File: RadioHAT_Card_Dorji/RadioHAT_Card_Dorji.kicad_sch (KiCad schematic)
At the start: 10 parts, among them J2 Conn_Coaxial, J3 Conn_Coaxial, J4 Conn_Coaxial, J5 Conn_Coaxial, J6 Conn_Coaxial

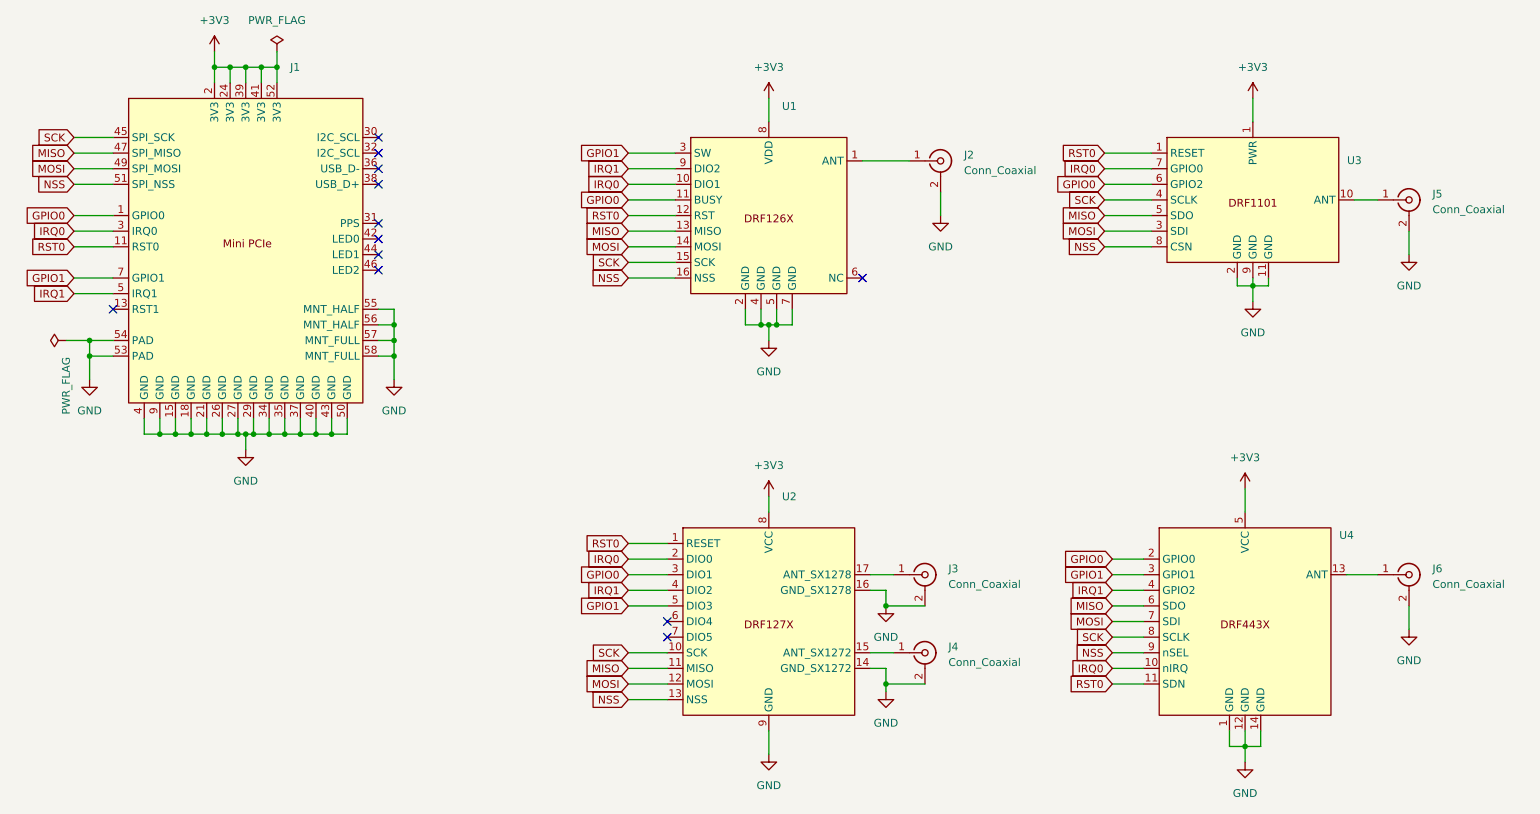
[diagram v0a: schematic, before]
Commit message: [PCB] Minor Dorji card fixes from rev0
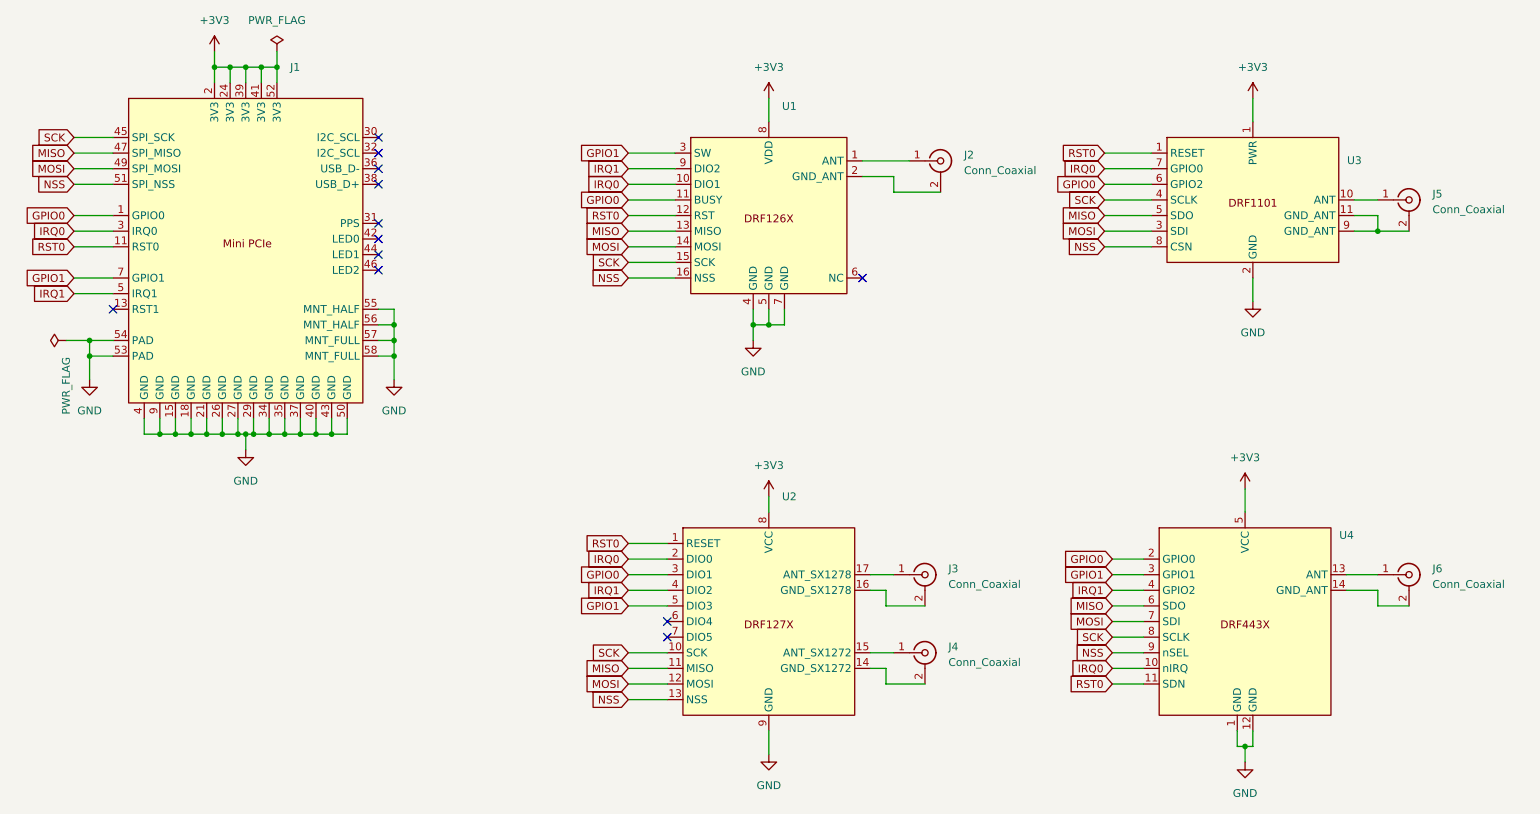
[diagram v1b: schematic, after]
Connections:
- net GND: no longer J2.2 (Ext), J3.2 (Ext), J4.2 (Ext), J5.2 (Ext), J6.2 (Ext), U1.2 (GND), U2.14 (GND_SX1272), U2.16 (GND_SX1278), U3.11 (GND), U3.9 (GND), U4.14 (GND)
- new net: J4.2 (Ext), U2.14 (GND_SX1272)
- new net: J3.2 (Ext), U2.16 (GND_SX1278)
- new net: J2.2 (Ext), U1.2 (GND_ANT)
- new net: J6.2 (Ext), U4.14 (GND_ANT)
- new net: J5.2 (Ext), U3.11 (GND_ANT), U3.9 (GND_ANT)

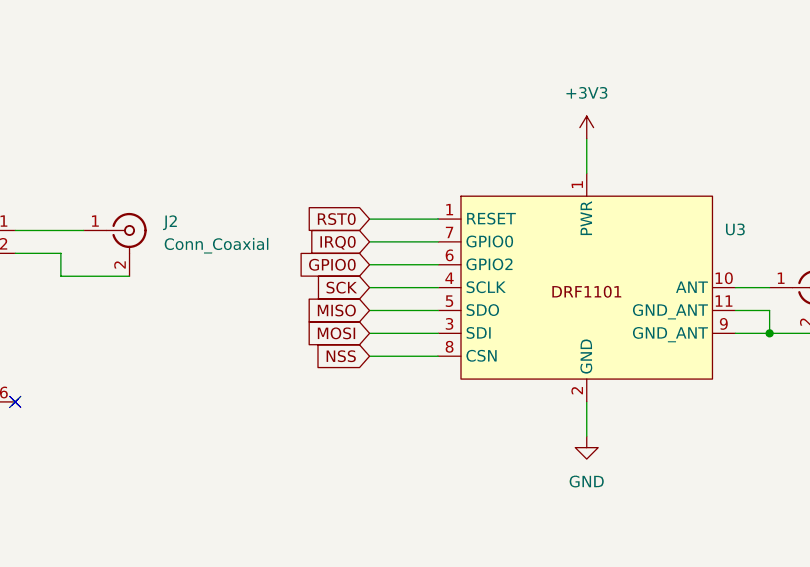
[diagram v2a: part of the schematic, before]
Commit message: Fix ERC issues
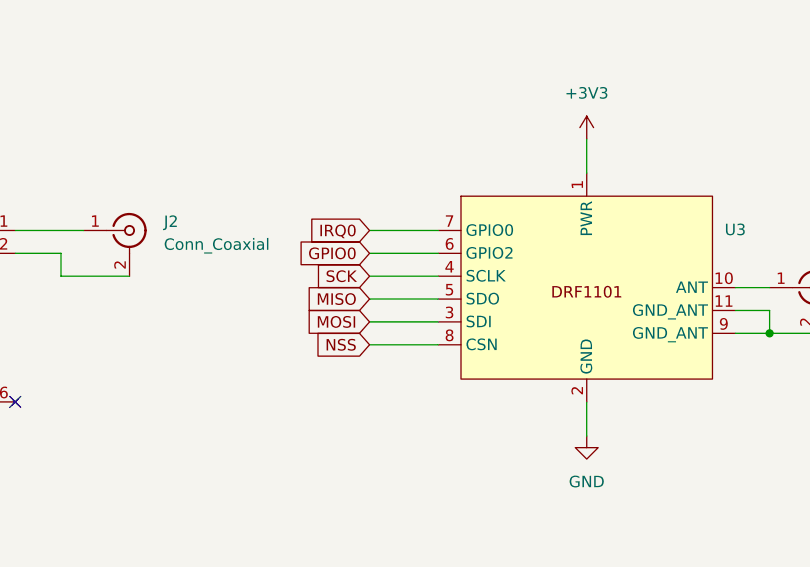
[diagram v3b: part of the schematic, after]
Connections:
- net RST0: no longer U3.1 (PWR)

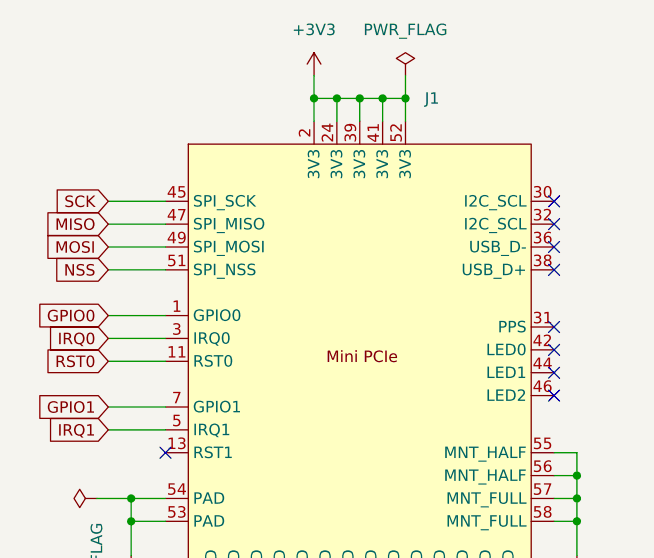
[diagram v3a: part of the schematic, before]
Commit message: Update symbols to align with library
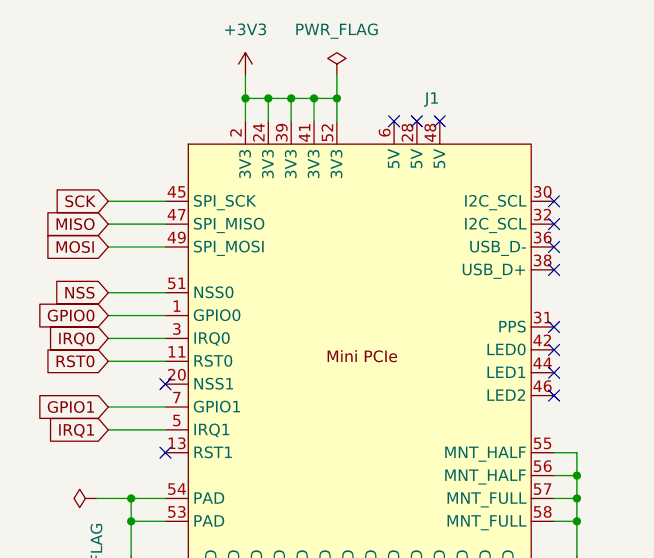
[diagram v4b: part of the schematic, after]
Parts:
- J1: Mouser (none) -> 571-1775838-2
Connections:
- no-connect marks 12 -> 16
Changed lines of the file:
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@@
 	(paper "A4")
 	(junction
-		(at 54.61 29.21)
-		(diameter 0)
-		(color 0 0 0 0)
-	)
-	(junction
 		(at 142.24 71.12)
 		(diameter 0)
@@
 	)
 	(junction
-		(at 62.23 29.21)
+		(at 52.07 29.21)
 		(diameter 0)
 		(color 0 0 0 0)
@@
 	)
 	(junction
-		(at 52.07 29.21)
-		(diameter 0)
-		(color 0 0 0 0)
-	)
-	(junction
-		(at 59.69 29.21)
+		(at 58.42 88.9)
 		(diameter 0)
 		(color 0 0 0 0)
 	)
 	(junction
-		(at 58.42 88.9)
+		(at 48.26 88.9)
 		(diameter 0)
 		(color 0 0 0 0)
 	)
 	(junction
-		(at 48.26 88.9)
+		(at 43.18 88.9)
 		(diameter 0)
 		(color 0 0 0 0)
 	)
 	(junction
-		(at 43.18 88.9)
+		(at 54.61 29.21)
 		(diameter 0)
 		(color 0 0 0 0)
 	)
 	(junction
-		(at 57.15 29.21)
+		(at 49.53 29.21)
 		(diameter 0)
 		(color 0 0 0 0)
@@
 	)
 	(junction
+		(at 46.99 29.21)
+		(diameter 0)
+		(color 0 0 0 0)
+	)
+	(junction
 		(at 55.88 88.9)
 		(diameter 0)
@@
 	)
 	(junction
+		(at 44.45 29.21)
+		(diameter 0)
+		(color 0 0 0 0)
+	)
+	(junction
 		(at 81.28 71.12)
 		(diameter 0)
@@
 	)
 	(no_connect
+		(at 66.04 31.75)
+	)
+	(no_connect
+		(at 60.96 31.75)
+	)
+	(no_connect
 		(at 78.74 59.69)
 	)
@@
 		(at 78.74 54.61)
 	)
+	(no_connect
+		(at 35.56 60.96)
+	)
+	(no_connect
+		(at 63.5 31.75)
+	)
 	(wire
 		(pts
@@
 	(wire
 		(pts
-			(xy 52.07 31.75) (xy 52.07 29.21)
+			(xy 49.53 29.21) (xy 46.99 29.21)
 		)
 		(stroke
@@
 	(wire
 		(pts
+			(xy 46.99 31.75) (xy 46.99 29.21)
+		)
+		(stroke
+			(width 0)
+			(type default)
+		)
+	)
+	(wire
+		(pts
 			(xy 58.42 86.36) (xy 58.42 88.9)
 		)
@@
 	(wire
 		(pts
-			(xy 62.23 26.67) (xy 62.23 29.21)
+			(xy 54.61 26.67) (xy 54.61 29.21)
 		)
 		(stroke
@@
 	(wire
 		(pts
-			(xy 29.21 48.26) (xy 35.56 48.26)
+			(xy 29.21 50.8) (xy 35.56 50.8)
 		)
 		(stroke
@@
 	(wire
 		(pts
-			(xy 54.61 29.21) (xy 57.15 29.21)
+			(xy 52.07 29.21) (xy 49.53 29.21)
 		)
 		(stroke
@@
 	(wire
 		(pts
+			(xy 54.61 31.75) (xy 54.61 29.21)
+		)
+		(stroke
+			(width 0)
+			(type default)
+		)
+	)
+	(wire
+		(pts
 			(xy 48.26 88.9) (xy 50.8 88.9)
 		)
@@
 	(wire
 		(pts
-			(xy 27.94 73.66) (xy 31.75 73.66)
+			(xy 44.45 26.67) (xy 44.45 29.21)
 		)
 		(stroke
@@
 	(wire
 		(pts
-			(xy 161.29 116.84) (xy 167.64 116.84)
+			(xy 27.94 73.66) (xy 31.75 73.66)
 		)
 		(stroke
@@
 	(wire
 		(pts
-			(xy 66.04 88.9) (xy 68.58 88.9)
+			(xy 161.29 116.84) (xy 167.64 116.84)
 		)
 		(stroke
@@
 	(wire
 		(pts
-			(xy 241.3 114.3) (xy 241.3 116.84)
+			(xy 66.04 88.9) (xy 68.58 88.9)
 		)
 		(stroke
@@
 	(wire
 		(pts
-			(xy 50.8 88.9) (xy 53.34 88.9)
+			(xy 241.3 114.3) (xy 241.3 116.84)
 		)
 		(stroke
@@
 	(wire
 		(pts
-			(xy 196.85 52.07) (xy 204.47 52.07)
+			(xy 50.8 88.9) (xy 53.34 88.9)
 		)
 		(stroke
@@
 	(wire
 		(pts
-			(xy 139.7 68.58) (xy 139.7 71.12)
+			(xy 196.85 52.07) (xy 204.47 52.07)
 		)
 		(stroke
@@
 	(wire
 		(pts
-			(xy 59.69 29.21) (xy 59.69 31.75)
+			(xy 139.7 68.58) (xy 139.7 71.12)
 		)
 		(stroke
@@
 	(wire
 		(pts
-			(xy 52.07 29.21) (xy 54.61 29.21)
+			(xy 46.99 29.21) (xy 44.45 29.21)
 		)
 		(stroke
@@
 	(wire
 		(pts
-			(xy 54.61 29.21) (xy 54.61 31.75)
-		)
-		(stroke
-			(width 0)
-			(type default)
-		)
-	)
-	(wire
-		(pts
 			(xy 29.21 43.18) (xy 35.56 43.18)
 		)
@@
 	(wire
 		(pts
-			(xy 57.15 29.21) (xy 59.69 29.21)
-		)
-		(stroke
-			(width 0)
-			(type default)
-		)
-	)
-	(wire
-		(pts
 			(xy 198.12 119.38) (xy 203.2 119.38)
 		)
@@
 	(wire
 		(pts
-			(xy 57.15 29.21) (xy 57.15 31.75)
-		)
-		(stroke
-			(width 0)
-			(type default)
-		)
-	)
-	(wire
-		(pts
-			(xy 52.07 26.67) (xy 52.07 29.21)
-		)
-		(stroke
-			(width 0)
-			(type default)
-		)
-	)
-	(wire
-		(pts
 			(xy 196.85 54.61) (xy 204.47 54.61)
 		)
@@
 	(wire
 		(pts
-			(xy 59.69 29.21) (xy 62.23 29.21)
-		)
-		(stroke
-			(width 0)
-			(type default)
-		)
-	)
-	(wire
-		(pts
 			(xy 237.49 53.34) (xy 241.3 53.34)
 		)
@@
 	(wire
 		(pts
-			(xy 62.23 29.21) (xy 62.23 31.75)
+			(xy 119.38 55.88) (xy 127 55.88)
 		)
 		(stroke
@@
 	(wire
 		(pts
-			(xy 119.38 55.88) (xy 127 55.88)
+			(xy 44.45 29.21) (xy 44.45 31.75)
 		)
 		(stroke
@@
 	(wire
 		(pts
+			(xy 49.53 31.75) (xy 49.53 29.21)
+		)
+		(stroke
+			(width 0)
+			(type default)
+		)
+	)
+	(wire
+		(pts
+			(xy 54.61 29.21) (xy 52.07 29.21)
+		)
+		(stroke
+			(width 0)
+			(type default)
+		)
+	)
+	(wire
+		(pts
 			(xy 119.38 48.26) (xy 127 48.26)
 		)
@@
 		)
 	)
+	(wire
+		(pts
+			(xy 52.07 31.75) (xy 52.07 29.21)
+		)
+		(stroke
+			(width 0)
+			(type default)
+		)
+	)
 	(global_label "NSS"
 		(shape input)
@@
 	(global_label "NSS"
 		(shape input)
-		(at 29.21 48.26 180)
+		(at 29.21 50.8 180)
 		(fields_autoplaced yes)
 		(effects
@@
 		)
 		(property "Intersheetrefs" "${INTERSHEET_REFS}"
-			(at 22.4753 48.26 0)
+			(at 22.4753 50.8 0)
 			(effects
 				(font
@@
 	(symbol
 		(lib_id "power:+3V3")
-		(at 52.07 26.67 0)
+		(at 44.45 26.67 0)
 		(unit 1)
 		(exclude_from_sim no)
@@
 		(fields_autoplaced yes)
 		(property "Reference" "#PWR04"
-			(at 52.07 30.48 0)
+			(at 44.45 30.48 0)
 			(effects
 				(font
@@
 		)
 		(property "Value" "+3V3"
-			(at 52.07 21.59 0)
+			(at 44.45 21.59 0)
 			(effects
 				(font
@@
 		)
 		(property "Footprint" ""
-			(at 52.07 26.67 0)
+			(at 44.45 26.67 0)
 			(effects
 				(font
@@
 		)
 		(property "Datasheet" ""
-			(at 52.07 26.67 0)
+			(at 44.45 26.67 0)
 			(effects
 				(font
@@
 		)
 		(property "Description" "Power symbol creates a global label with name \"+3V3\""
-			(at 52.07 26.67 0)
+			(at 44.45 26.67 0)
 			(effects
 				(font
@@
 	(symbol
 		(lib_id "power:PWR_FLAG")
-		(at 62.23 26.67 0)
+		(at 54.61 26.67 0)
 		(unit 1)
 		(exclude_from_sim no)
@@
 		(fields_autoplaced yes)
 		(property "Reference" "#FLG01"
-			(at 62.23 24.765 0)
+			(at 54.61 24.765 0)
 			(effects
 				(font
@@
 		)
 		(property "Value" "PWR_FLAG"
-			(at 62.23 21.59 0)
+			(at 54.61 21.59 0)
 			(effects
 				(font
@@
 		)
 		(property "Footprint" ""
-			(at 62.23 26.67 0)
+			(at 54.61 26.67 0)
 			(effects
 				(font
@@
 		)
 		(property "Datasheet" "~"
-			(at 62.23 26.67 0)
+			(at 54.61 26.67 0)
 			(effects
 				(font
@@
 		)
 		(property "Description" "Special symbol for telling ERC where power comes from"
-			(at 62.23 26.67 0)
+			(at 54.61 26.67 0)
 			(effects
 				(font
@@
 		(on_board yes)
 		(dnp no)
-		(fields_autoplaced yes)
 		(property "Reference" "J1"
 			(at 64.3733 29.21 0)
@@
 			)
 		)
+		(property "Mouser" "571-1775838-2"
+			(at 57.404 60.198 0)
+			(effects
+				(font
+					(size 1.27 1.27)
+				)
+				(hide yes)
+			)
+		)
 		(pin "51"
 		)
@@
 		(pin "45"
 		)
+		(pin "20"
+		)
+		(pin "6"
+		)
+		(pin "28"
+		)
+		(pin "48"
+		)
 		(instances
